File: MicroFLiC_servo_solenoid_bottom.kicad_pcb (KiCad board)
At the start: 2 copper layers, 49.8 x 49.8 mm, 37 parts, among them P1 1x14 header strip, P10 1x4 socket strip, P11 2x3 header strip R/A, P12 2x3 header strip R/A, P2 1x14 socket strip, P3 12-way Micro-MaTch, P4 Jack_3.5mm_3pin, P5 Jack_3.5mm_3pin, P6 RCA_3, P7 RCA_3, P8 1x6 socket strip, P9 1x4 header strip, U1 PCA9306DP, U2 DRV103, U3 DRV103, U4 MCP4728

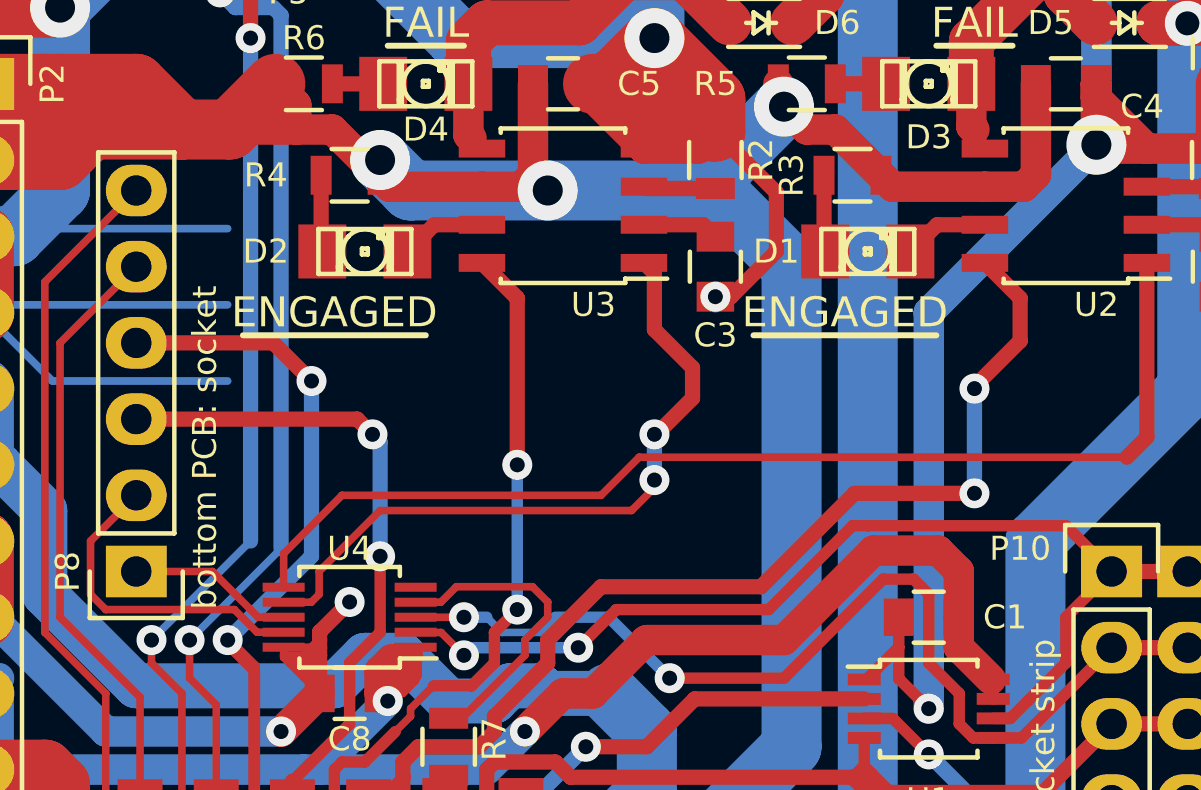
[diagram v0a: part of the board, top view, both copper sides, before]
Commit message: Added board name, created new Gerber plots
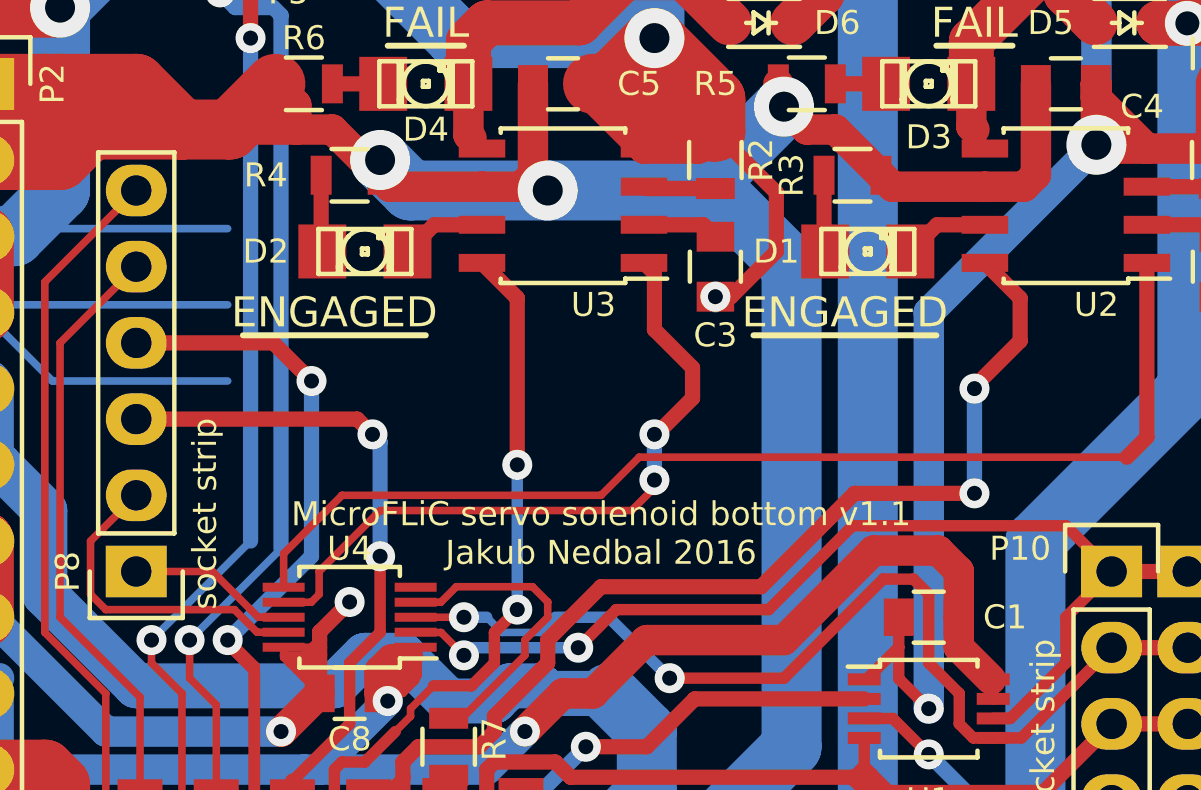
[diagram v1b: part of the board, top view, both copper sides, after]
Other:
- board text added: "MicroFLiC servo solenoid bottom v1.1 Jakub Nedbal 2016"
- board text removed: "bottom PCB: socket"
- board text removed: "top PCB: pin header"
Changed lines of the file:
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@@
     (links 119)
     (no_connects 0)
-    (area 100.025999 100.025999 149.910001 149.910001)
+    (area 97.001475 90.746999 153.474335 155.211001)
     (thickness 1.6)
-    (drawings 29)
+    (drawings 30)
     (tracks 723)
     (zones 0)
@@
   (page A4)
   (layers
-    (0 F.Cu signal)
+    (0 F.Cu signal hide)
     (31 B.Cu signal)
     (32 B.Adhes user)
@@
   )
   (setup
-    (last_trace_width 0.508)
+    (last_trace_width 0.254)
     (user_trace_width 0.254)
     (user_trace_width 0.381)
@@
     )
   )
+  (gr_text "MicroFLiC servo solenoid bottom v1.1\nJakub Nedbal 2016" (at 127.254 130.302) (layer F.SilkS)
+    (effects (font (size 0.8 0.8) (thickness 0.12)))
+  )
+  (gr_text "MicroFLiC servo solenoid bottom v1.1\nJakub Nedbal 2016" (at 127.254 130.302) (layer B.SilkS)
+    (effects (font (size 0.8 0.8) (thickness 0.12)) (justify mirror))
+  )
   (gr_text "header strip" (at 148.844 140.208 90) (layer B.SilkS)
     (effects (font (size 0.8 0.8) (thickness 0.12)) (justify right mirror))
@@
     (effects (font (size 0.8 0.8) (thickness 0.12)) (justify left))
   )
-  (gr_text "bottom PCB: socket" (at 114.046 132.842 90) (layer F.SilkS)
+  (gr_text "socket strip" (at 114.046 132.842 90) (layer F.SilkS)
     (effects (font (size 0.8 0.8) (thickness 0.12)) (justify left))
   )
-  (gr_text "top PCB: pin header" (at 114.046 132.842 90) (layer B.SilkS)
-    (effects (font (size 0.8 0.8) (thickness 0.12)) (justify right mirror))
-  )
   (gr_text "header strip" (at 101.854 149.098 90) (layer B.SilkS)

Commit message: Fixed jack part values
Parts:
- P4, P5: value Jack_3.5mm_3pin -> 3.5mm jack
- P6, P7: value RCA_3 -> RCA jack
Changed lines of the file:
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@@
     (links 119)
     (no_connects 0)
-    (area 97.001475 90.746999 153.474335 155.211001)
+    (area 100.025999 100.025999 149.910001 149.910001)
     (thickness 1.6)
     (drawings 30)
@@
       (effects (font (size 0.8 0.8) (thickness 0.12)))
     )
-    (fp_text value RCA_3 (at -1.016 0 360) (layer F.SilkS) hide
+    (fp_text value "RCA jack" (at -1.016 0 360) (layer F.SilkS) hide
       (effects (font (size 1 1) (thickness 0.15)))
     )
@@
       (effects (font (size 0.8 0.8) (thickness 0.12)))
     )
-    (fp_text value RCA_3 (at 0 6.35 270) (layer F.SilkS) hide
+    (fp_text value "RCA jack" (at 0 6.35 270) (layer F.SilkS) hide
       (effects (font (size 1 1) (thickness 0.15)))
     )
@@
       (effects (font (size 0.8 0.8) (thickness 0.12)))
     )
-    (fp_text value Jack_3.5mm_3pin (at 9.525 0 360) (layer F.SilkS) hide
+    (fp_text value "3.5mm jack" (at 9.525 0 360) (layer F.SilkS) hide
       (effects (font (size 1 1) (thickness 0.15)))
     )
@@
       (effects (font (size 0.8 0.8) (thickness 0.12)))
     )
-    (fp_text value Jack_3.5mm_3pin (at 9.525 0 360) (layer F.SilkS) hide
-      (effects (font (size 1 1) (thickness 0.15)))
-    )
+    (fp_text value "3.5mm jack" (at 9.525 0 360) (layer F.SilkS) hide
+      (effects (font (size 1 1) (thickness 0.15)))
+    )

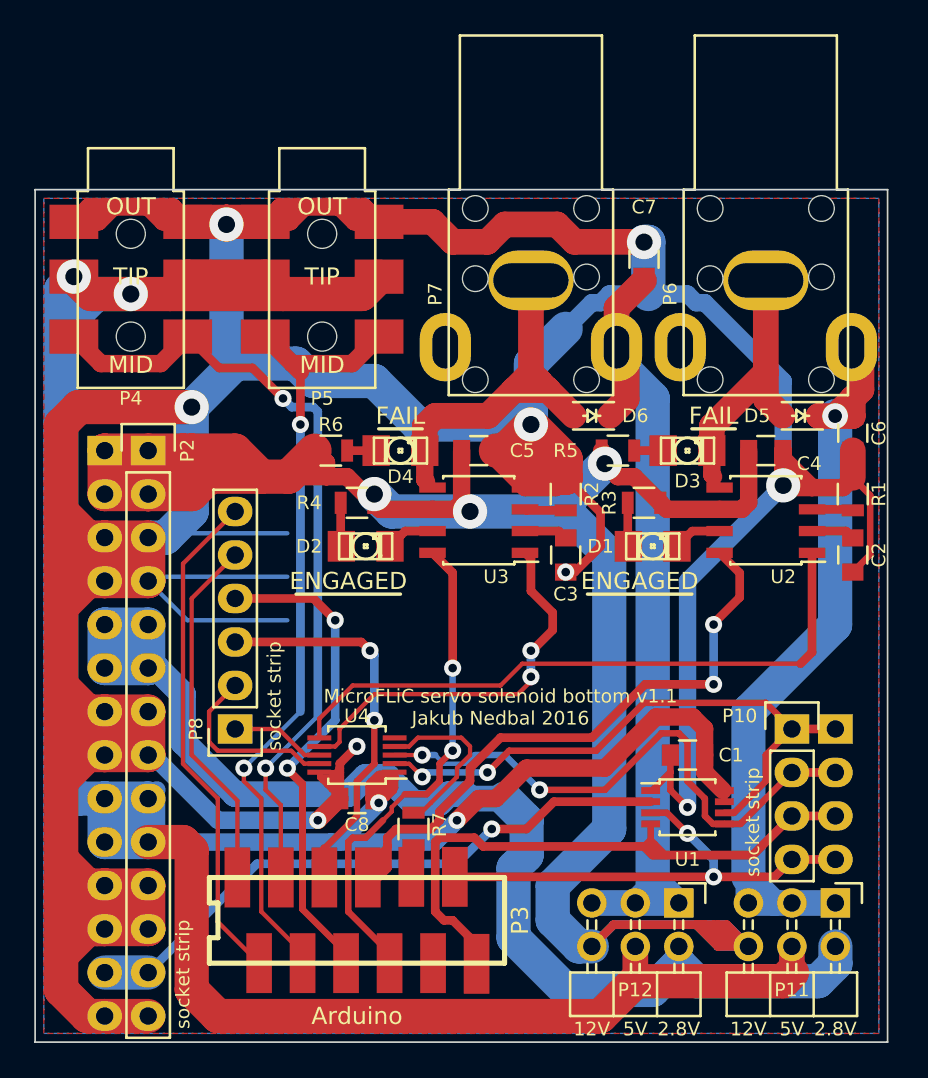
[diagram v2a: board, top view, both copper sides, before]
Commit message: Added pullup resistors to I2C
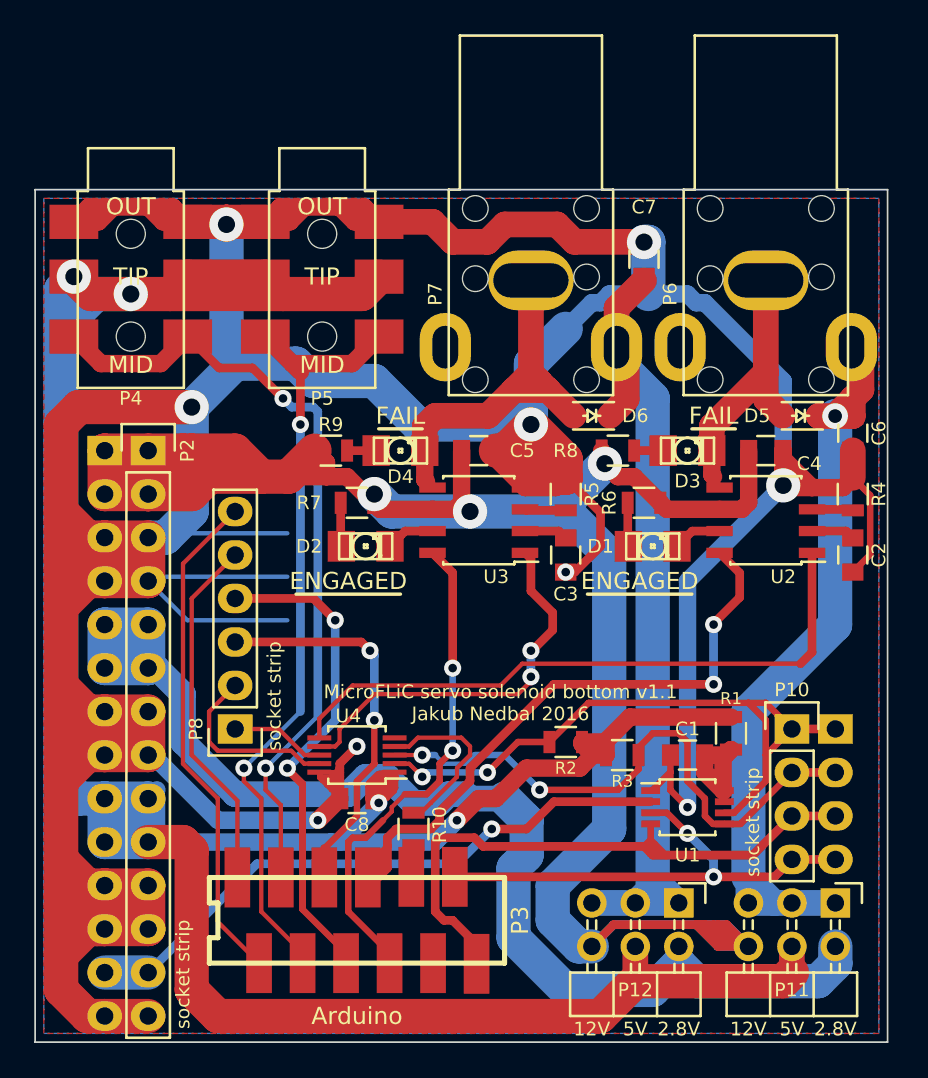
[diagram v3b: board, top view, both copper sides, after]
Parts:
- added R1: 270k, Resistors_SMD:R_0805, F.Cu at (140.7, 131.8)
- added R2: 1k5, Resistors_SMD:R_0805, F.Cu at (131.1, 132.3)
- added R3: 1k5, Resistors_SMD:R_0805, F.Cu at (134.4, 133.1)
- renumbered R7 to R10, R1 to R4, R2 to R5, R3 to R6, R4 to R7, R5 to R8, R6 to R9
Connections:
- C1 pad 1: +5VP -> Net-(C1-Pad1)
- U1 pad 7: +5VP -> Net-(C1-Pad1)
- U1 pad 8: +5VP -> Net-(C1-Pad1)
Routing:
- net Net-(C1-Pad1): track 0.00 -> 7.58 mm
- net /I2C/SCL_5V: track 35.7 -> 39.2 mm
- net /I2C/SDA_5V: track 33.7 -> 34.5 mm

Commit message: Changed ENGAGED LED anode to +5V, changed SOD-323 packages.
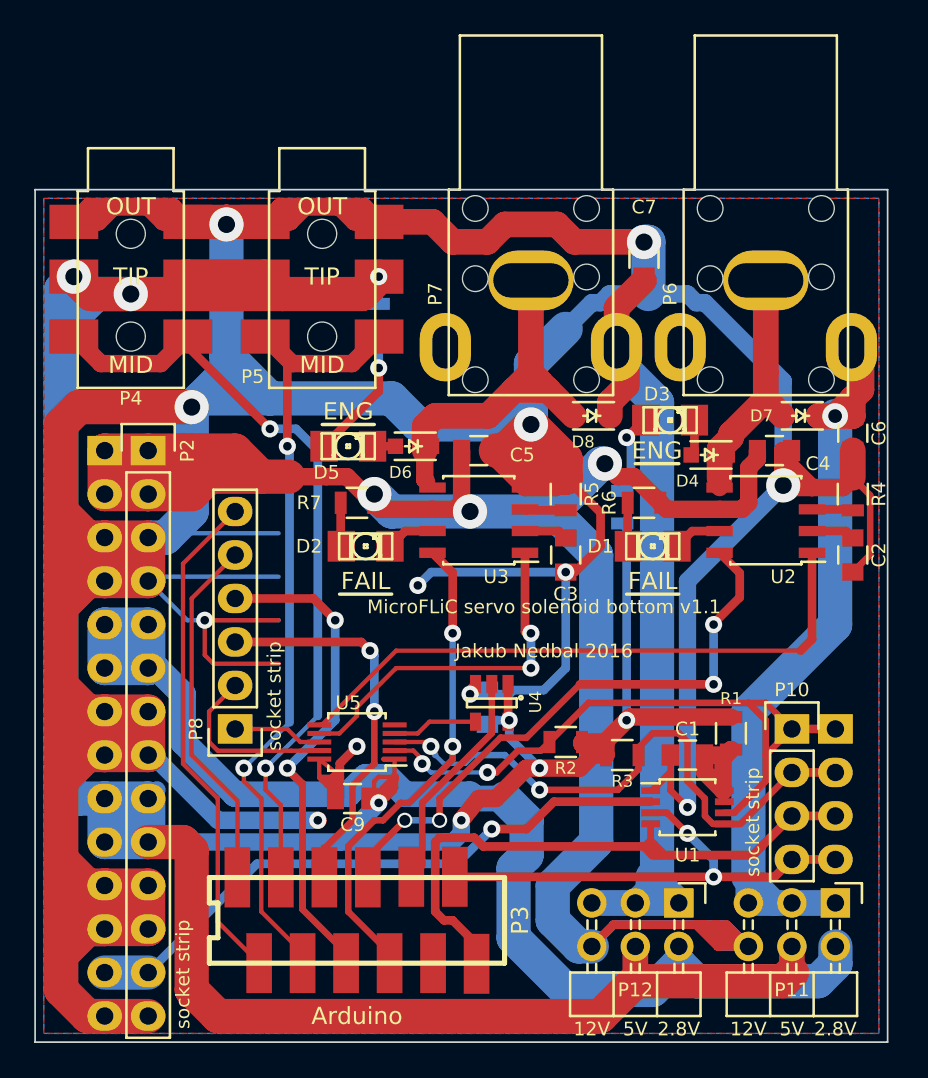
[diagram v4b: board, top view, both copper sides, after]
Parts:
- removed the D5 at (144.8, 113.3)
- removed R10: 0R, Resistors_SMD:R_0805
- added C8: 100n, Capacitors_SMD:C_0805, B.Cu at (126.5, 130.3)
- added D4: 1N4148, jakub:SOD-323, F.Cu at (139.4, 115.6)
- added D7: 1N4148, jakub:SOD-323, F.Cu at (144.8, 113.3)
- added D8: 1N4148, jakub:SOD-323, F.Cu at (132.6, 113.3)
- added U4: 74HCT1G125, TO_SOT_Packages_SMD:SOT-23-5, F.Cu at (126.7, 130.0)
- D6: footprint Diodes_SMD:SOD-323 -> jakub:SOD-323
- R8, R9: value 10k -> 3k; moved to B.Cu
- moved D6 10.6 mm to (122.2, 115.1)
- moved R9 8.12 mm to (120.1, 107.7), turned to 90 degrees
- moved R8 3.31 mm to (134.4, 118.6), turned to 270 degrees
- moved D5 3.06 mm to (118.4, 115.1)
- moved D3 2.05 mm to (137.2, 113.5)
- moved U5 0.76 mm to (118.9, 132.3)
- moved C4 0.51 mm to (143.3, 115.3)
- moved C9 0.25 mm to (118.6, 135.6)
- renumbered C8 to C9, D4 to D5, U4 to U5
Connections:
- net /shutterPWM/ENG_A renamed /shutterPWM/FAIL_A
- net /shutterPWM/ENG_B renamed /shutterPWM/FAIL_B
- D1 pad 2: /shutterPWM/EA -> /shutterPWM/FA
- D2 pad 2: /shutterPWM/EB -> /shutterPWM/FB
- D3 pad 1: /shutterPWM/SHA_O/C -> /shutterPWM/EA2
- D3 pad 2: /shutterPWM/FA -> /shutterPWM/EA1
- D5 pad 1: /shutterPWM/SHB_O/C -> /shutterPWM/EB2
- D5 pad 2: /shutterPWM/FB -> /shutterPWM/EB1
- D6 pad 1: /shutterPWM/SHB_PWR -> /shutterPWM/SHB_O/C
- D6 pad 2: /shutterPWM/SHB_O/C -> /shutterPWM/EB2
- R6 pad 1: /shutterPWM/EA -> /shutterPWM/FA
- R7 pad 1: /shutterPWM/EB -> /shutterPWM/FB
- R8 pad 1: /shutterPWM/FA -> /shutterPWM/EA1
- R8 pad 2: +12V -> +5VP
- R9 pad 1: /shutterPWM/FB -> /shutterPWM/EB1
- R9 pad 2: +12V -> +5VP
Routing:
- net GND: track 356.6 -> 391.8 mm, vias 9 -> 12
- net +5VP: track 187.1 -> 206.7 mm, vias 4 -> 8
- net /shutterPWM/SH_~LDAC: track 1.90 -> 13.2 mm
- net /shutterPWM/EB1: track 0.00 -> 7.74 mm, vias 0 -> 1
- net Net-(U4-Pad4): track 10.3 -> 4.75 mm
- net /shutterPWM/SH1: track 40.4 -> 35.1 mm, vias 2 -> 4
- net +12V: track 155.2 -> 149.9 mm
- net /shutterPWM/EA1: track 0.00 -> 4.97 mm, vias 0 -> 1
- net /shutterPWM/SHB_PWR: track 49.2 -> 53.1 mm
- net /shutterPWM/EA2: track 0.00 -> 2.68 mm
- net /shutterPWM/EB: track 2.61 -> 0.00 mm
- net /shutterPWM/EA: track 2.56 -> 0.00 mm
- net /shutterPWM/SH2_PWM: track 23.2 -> 21.6 mm
- net /shutterPWM/SH1_PWM: track 37.5 -> 36.0 mm
- net /SERVO1: track 46.8 -> 45.5 mm
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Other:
- board text added: "ENG"
- board text removed: "ENGAGED"

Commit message: Changed 100n->100p capacitor on the I2C level shifter
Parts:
- C1: value 100n -> 100p
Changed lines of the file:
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@@
       (effects (font (size 0.8 0.8) (thickness 0.12)))
     )
-    (fp_text value 100n (at 0 2.1 180) (layer F.Fab) hide
+    (fp_text value 100p (at 0 2.1 180) (layer F.Fab) hide
       (effects (font (size 1 1) (thickness 0.15)))
     )
